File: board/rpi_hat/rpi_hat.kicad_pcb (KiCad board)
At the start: 2 copper layers, 70.5 x 69.8 mm, 9 parts, among them J1 DB9_Male, J2 DB9_Male, J3 Raspberry_Pi_2_3

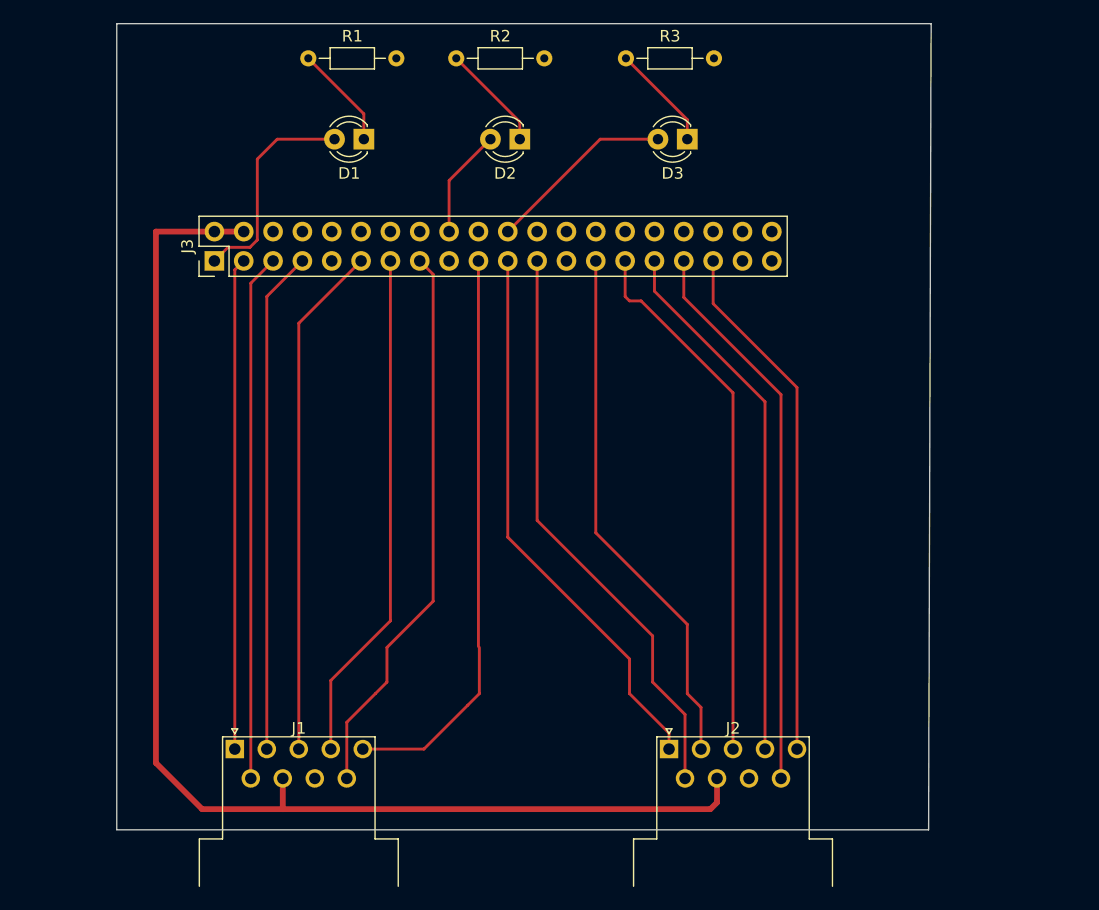
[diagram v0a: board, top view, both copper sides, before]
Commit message: rpi hat: rev A
Routing re done to make it easier to use
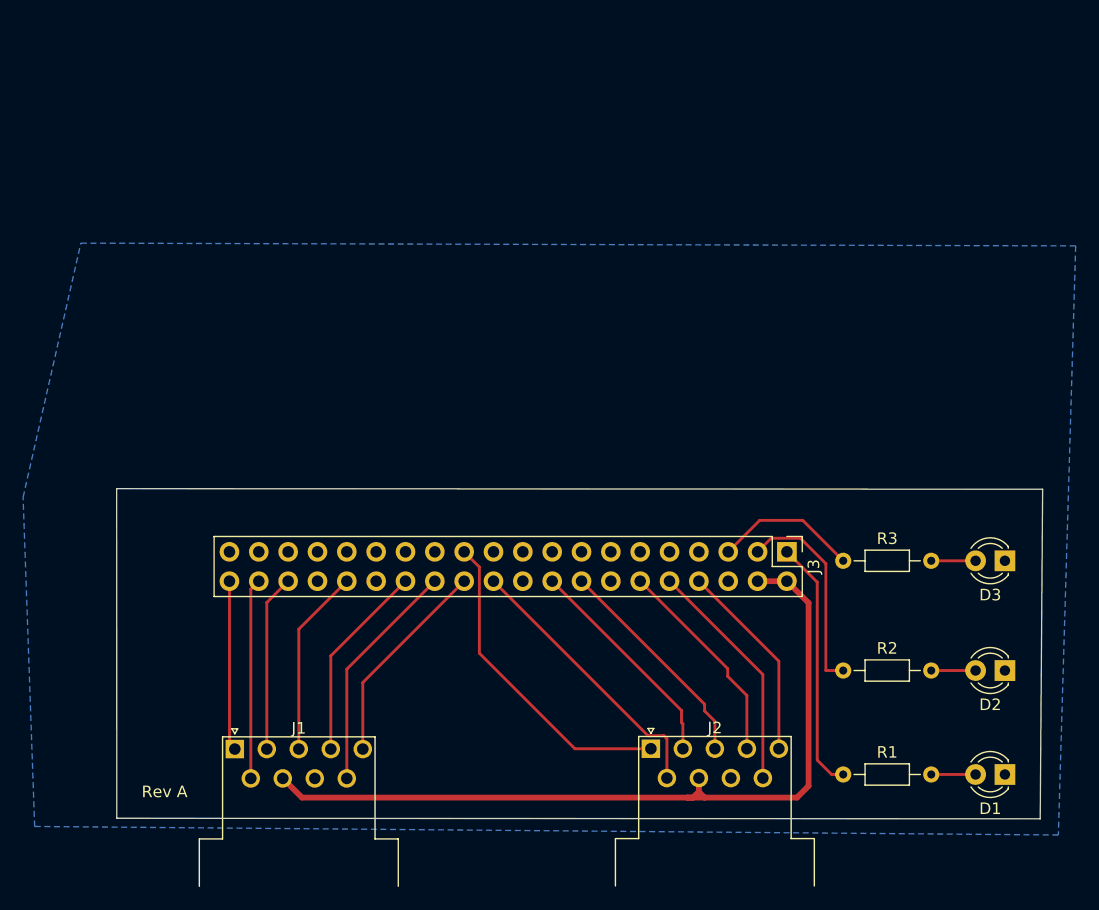
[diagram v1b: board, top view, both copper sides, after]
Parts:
- moved D1 78.1 mm to (164.5, 94.0)
- moved R1 77.4 mm to (150.5, 94.0)
- moved R2 62.7 mm to (150.5, 85.0)
- moved D2 62.3 mm to (164.5, 85.0)
- moved J3 55.6 mm to (145.6, 74.7), turned to -90 degrees
- moved R3 47.4 mm to (150.5, 75.5)
- moved D3 45.7 mm to (164.5, 75.5)
- moved J2 1.57 mm to (133.8, 91.8)
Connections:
- D1 pad 1: Net-(D1-Pad1) -> GND
- D1 pad 2: /LED_PWR -> Net-(R1-Pad2)
- D2 pad 1: Net-(D2-Pad1) -> GND
- D2 pad 2: /LED_1 -> Net-(R2-Pad2)
- D3 pad 1: Net-(D3-Pad1) -> GND
- D3 pad 2: /LED_2 -> Net-(D3-Pad2)
- J1 pad 5: /J1_POTX -> /J1_FIRE3
- J1 pad 9: /J1_POTY -> /J1_FIRE2
- J2 pad 5: /J2_POTX -> /J2_FIRE3
- J2 pad 9: /J2_POTY -> /J2_FIRE2
- J3 pad 10: unconnected-(J3-Pad10) -> /J2_FIRE2
- J3 pad 11: /J1_LEFT -> unconnected-(J3-Pad11)
- J3 pad 12: unconnected-(J3-Pad12) -> /J2_RIGHT
- J3 pad 13: /J1_RIGHT -> unconnected-(J3-Pad13)
- J3 pad 15: /J1_POTY -> unconnected-(J3-Pad15)
- J3 pad 16: unconnected-(J3-Pad16) -> /J2_LEFT
- J3 pad 18: /LED_1 -> /J2_DOWN
- J3 pad 19: /J1_POTX -> unconnected-(J3-Pad19)
- J3 pad 21: /J2_UP -> unconnected-(J3-Pad21)
- J3 pad 22: /LED_2 -> /J2_FIRE
- J3 pad 23: /J2_FIRE -> /J2_UP
- J3 pad 24: unconnected-(J3-Pad24) -> /J1_FIRE3
- J3 pad 26: unconnected-(J3-Pad26) -> /J1_FIRE2
- J3 pad 27: /J2_DOWN -> unconnected-(J3-Pad27)
- J3 pad 28: unconnected-(J3-Pad28) -> /J1_RIGHT
- J3 pad 29: /J2_LEFT -> unconnected-(J3-Pad29)
- J3 pad 3: /J1_UP -> /LED_1
- J3 pad 31: /J2_RIGHT -> unconnected-(J3-Pad31)
- J3 pad 32: unconnected-(J3-Pad32) -> /J1_LEFT
- J3 pad 33: /J2_POTY -> unconnected-(J3-Pad33)
- J3 pad 35: /J2_POTX -> unconnected-(J3-Pad35)
- J3 pad 36: unconnected-(J3-Pad36) -> /J1_DOWN
- J3 pad 38: unconnected-(J3-Pad38) -> /J1_FIRE
- J3 pad 40: unconnected-(J3-Pad40) -> /J1_UP
- J3 pad 5: /J1_FIRE -> /LED_2
- J3 pad 7: /J1_DOWN -> unconnected-(J3-Pad7)
- J3 pad 8: unconnected-(J3-Pad8) -> /J2_FIRE3
- R1 pad 1: Net-(D1-Pad1) -> /LED_PWR
- R1 pad 2: GND -> Net-(R1-Pad2)
- R2 pad 1: Net-(D2-Pad1) -> /LED_1
- R2 pad 2: GND -> Net-(R2-Pad2)
- R3 pad 1: Net-(D3-Pad1) -> /LED_2
- R3 pad 2: GND -> Net-(D3-Pad2)
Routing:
- net /J1_POTX: track 49.5 -> 0.00 mm
- net /J1_POTY: track 48.4 -> 0.00 mm
- net /J2_POTY: track 48.3 -> 0.00 mm
- net /J2_POTX: track 45.3 -> 0.00 mm
- net +5V: track 108.8 -> 70.8 mm
- net /J1_DOWN: track 43.5 -> 15.3 mm
- net /J1_LEFT: track 44.5 -> 16.3 mm
- net /J1_FIRE: track 45.6 -> 17.4 mm
- net /J2_RIGHT: track 46.2 -> 18.3 mm
- net /J1_UP: track 42.6 -> 14.7 mm
- net /J2_LEFT: track 46.7 -> 19.3 mm
- net /J1_RIGHT: track 44.4 -> 17.2 mm
- net /J2_DOWN: track 46.0 -> 19.2 mm
- net /J2_FIRE: track 50.1 -> 24.1 mm
- net /J2_UP: track 48.0 -> 27.6 mm
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- added copper zone on B.Cu, net GND
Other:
- board size 70.5 x 69.8 mm -> 80.2 x 28.6 mm
- board text added: "Rev A"
